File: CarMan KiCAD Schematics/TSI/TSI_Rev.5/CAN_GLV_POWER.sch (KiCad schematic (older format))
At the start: 52 parts, among them J31 Cooling Jumper, K2 G5LE-1-E, K3 SFS2-DC24V, K4 SFS2-DC24V, Q11 TN2130K1-G, U14 Bottom Left, U15 Top Left, U17 Top Right, U2 Bottom Right, U20 TLP293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

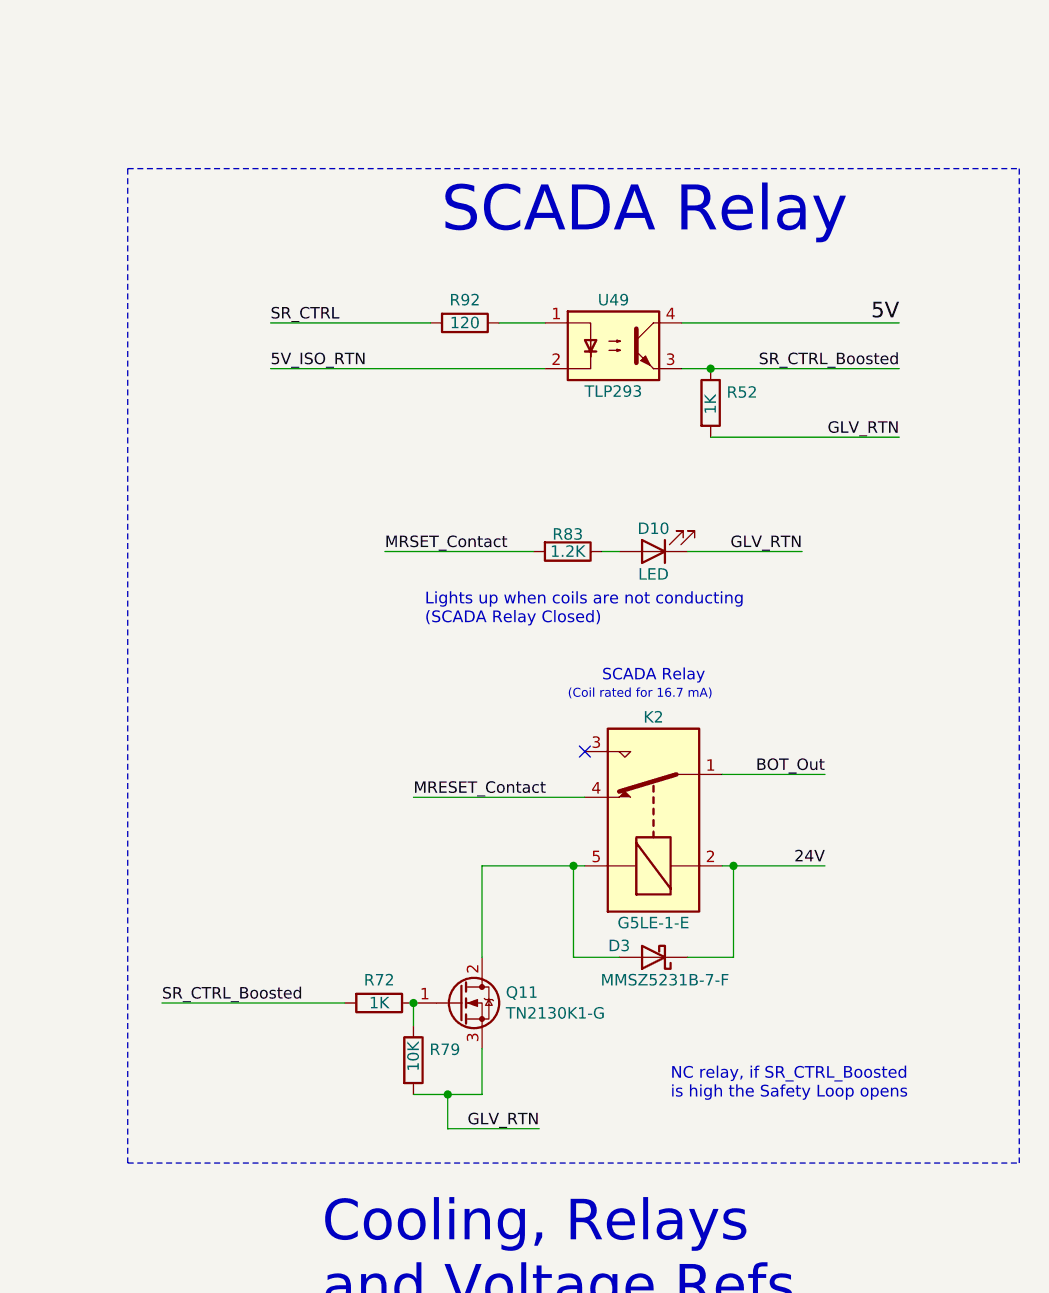
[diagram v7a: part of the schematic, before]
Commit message: - SR Control boosted and scada relay circuit edited
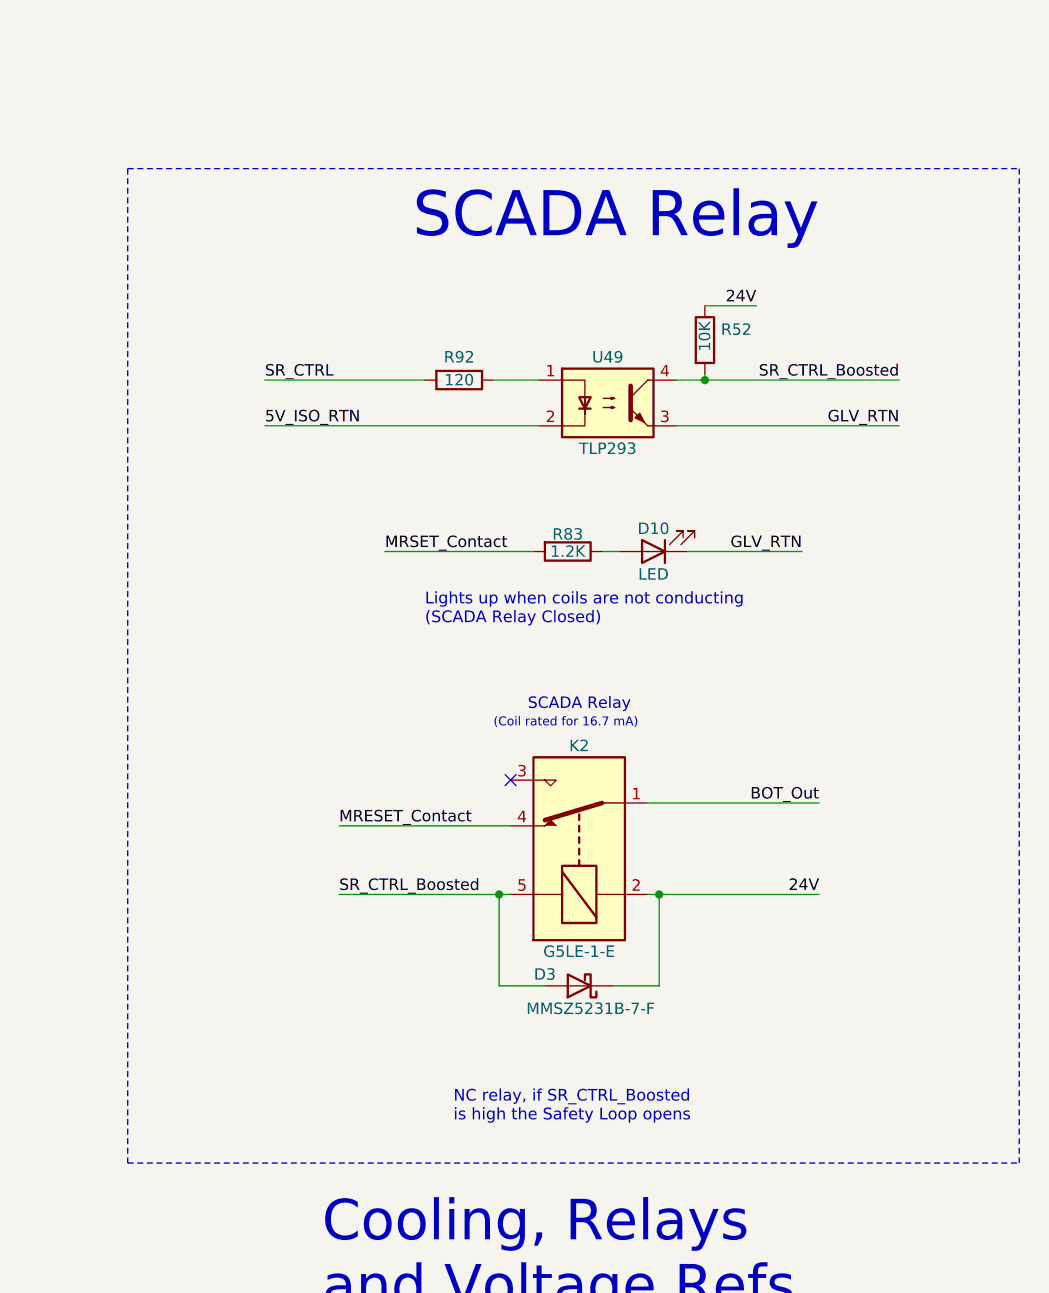
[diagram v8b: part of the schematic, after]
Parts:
- removed Q11: TN2130K1-G, TSI_Rev_2021_Footprint_Lib:SOT95P237X112-3N, symbol Device:Q_NMOS_GDS
- removed R72: 1K, Resistor_SMD:R_0805_2012Metric_Pad1.15x1.40mm_HandSolder, symbol Device:R
- removed R79: 10K, Resistor_SMD:R_0805_2012Metric_Pad1.15x1.40mm_HandSolder, symbol Device:R
- R52: value 1K -> 10K
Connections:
- wire segments 204 -> 197
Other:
- moved on the sheet: D3, K2, R52, R92, U49
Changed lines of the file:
@@
 Text Notes 12900 10500 0    177  ~ 0
 Cooling, Relays \nand Voltage Refs\n
-Text Label 12675 6175 0    50   ~ 0
+Text Label 12650 6425 0    50   ~ 0
 SR_CTRL
 $Comp
 L Device:D_Schottky D3
 U 1 1 5FB8F043
-P 14350 8950
-F 0 "D3" H 14500 8900 50  0000 C CNN
-F 1 "MMSZ5231B-7-F" H 14300 9050 50  0000 C CNN
-F 2 "Diode_SMD:D_SOD-123" H 14350 8950 50  0001 C CNN
-F 3 "~" H 14350 8950 50  0001 C CNN
-	1    14350 8950
+P 14025 9075
+F 0 "D3" H 14175 9025 50  0000 C CNN
+F 1 "MMSZ5231B-7-F" H 13975 9175 50  0000 C CNN
+F 2 "Diode_SMD:D_SOD-123" H 14025 9075 50  0001 C CNN
+F 3 "~" H 14025 9075 50  0001 C CNN
+	1    14025 9075
 	-1   0    0    1
 $EndComp
 Wire Wire Line
-	14650 8550 14700 8550
-NoConn ~ 14050 8050
+	14325 8675 14375 8675
+NoConn ~ 13725 8175
 Text Notes 14800 750  0    98   ~ 0
 SIGNALS
@@
 Wire Notes Line
 	2250 3950 4000 3950
-Text Label 12675 6375 0    50   ~ 0
+Text Label 12650 6625 0    50   ~ 0
 5V_ISO_RTN
 $Comp
 L TSI_Rev.5-rescue:TLP293-CarMan_KiCAD_Library-TSI_Rev.5-rescue U49
 U 1 1 5FA61B5B
-P 14175 6275
-F 0 "U49" H 14175 6475 50  0000 C CNN
-F 1 "TLP293" H 14175 6075 50  0000 C CNN
-F 2 "Package_SO:SOIC-4_4.55x2.6mm_P1.27mm" H 13975 6075 50  0001 L CIN
-F 3 "" H 14175 6275 50  0001 L CNN
-	1    14175 6275
-	1    0    0    -1
-$EndComp
-Wire Wire Line
-	13875 6175 13675 6175
+P 14150 6525
+F 0 "U49" H 14150 6725 50  0000 C CNN
+F 1 "TLP293" H 14150 6325 50  0000 C CNN
+F 2 "Package_SO:SOIC-4_4.55x2.6mm_P1.27mm" H 13950 6325 50  0001 L CIN
+F 3 "" H 14150 6525 50  0001 L CNN
+	1    14150 6525
+	1    0    0    -1
+$EndComp
+Wire Wire Line
+	13850 6425 13650 6425
 $Comp
 L Device:R R92
 U 1 1 5FA61B65
-P 13525 6175
-F 0 "R92" V 13425 6175 50  0000 C CNN
-F 1 "120" V 13525 6175 50  0000 C CNN
-F 2 "Resistor_SMD:R_0805_2012Metric_Pad1.15x1.40mm_HandSolder" V 13455 6175 50  0001 C CNN
-F 3 "~" H 13525 6175 50  0001 C CNN
-	1    13525 6175
+P 13500 6425
+F 0 "R92" V 13400 6425 50  0000 C CNN
+F 1 "120" V 13500 6425 50  0000 C CNN
+F 2 "Resistor_SMD:R_0805_2012Metric_Pad1.15x1.40mm_HandSolder" V 13430 6425 50  0001 C CNN
+F 3 "~" H 13500 6425 50  0001 C CNN
+	1    13500 6425
 	0    1    1    0
 $EndComp
-Text Notes 14125 7750 0    50   ~ 0
+Text Notes 13800 7875 0    50   ~ 0
 SCADA Relay\n
-$Comp
-L Device:Q_NMOS_GDS Q11
-U 1 1 5FB4C495
-P 13500 9150
-F 0 "Q11" H 13704 9196 50  0000 L CNN
-F 1 "TN2130K1-G" H 13704 9105 50  0000 L CNN
-F 2 "TSI_Rev_2021_Footprint_Lib:SOT95P237X112-3N" H 13700 9250 50  0001 C CNN
-F 3 "https://ww1.microchip.com/downloads/en/DeviceDoc/TN2130-N-Channel-Enhancement-Mode-Vertical-DMOS-FET-Data-Sheet-20005944B.pdf" H 13500 9150 50  0001 C CNN
-	1    13500 9150
-	1    0    0    -1
-$EndComp
-Text Label 12200 9150 0    50   ~ 0
+Text Label 12975 8675 0    50   ~ 0
 SR_CTRL_Boosted
 $Comp
@@
 Text Label 3350 1250 0    50   ~ 0
 5V_ISO_RTN
-Text Label 13300 8250 0    50   ~ 0
+Text Label 12975 8375 0    50   ~ 0
 MRESET_Contact
 Text Notes 6275 800  2    89   ~ 0
 Cooling Control & Sensors\n
-$Comp
-L Device:R R72
-U 1 1 5FB6696B
-P 13150 9150
-F 0 "R72" V 13050 9150 50  0000 C CNN
-F 1 "1K" V 13150 9150 50  0000 C CNN
-F 2 "Resistor_SMD:R_0805_2012Metric_Pad1.15x1.40mm_HandSolder" V 13080 9150 50  0001 C CNN
-F 3 "~" H 13150 9150 50  0001 C CNN
-	1    13150 9150
-	0    1    1    0
-$EndComp
-Wire Wire Line
-	13300 9150 13300 9250
-Text Label 13850 9700 2    50   ~ 0
-GLV_RTN
-Connection ~ 13300 9150
-Wire Wire Line
-	13600 9350 13600 9550
-Wire Wire Line
-	13600 9550 13450 9550
-Wire Wire Line
-	13600 8950 13600 8550
-Text Label 15100 8550 2    50   ~ 0
+Text Label 15075 8675 2    50   ~ 0
 24V
 Wire Wire Line
-	14500 8950 14700 8950
-Connection ~ 14700 8550
-Wire Wire Line
-	14200 8950 14000 8950
-Connection ~ 14000 8550
-Wire Wire Line
-	14000 8550 14050 8550
+	14175 9075 14375 9075
+Wire Wire Line
+	13875 9075 13675 9075
+Wire Wire Line
+	13675 8675 13725 8675
 Text Notes 11050 11200 0    39   ~ 0
 Zacky Bear Doesn't Like
@@
 L Device:R R52
 U 1 1 5FC2D02C
-P 14600 6525
-F 0 "R52" H 14670 6571 50  0000 L CNN
-F 1 "1K" V 14600 6475 50  0000 L CNN
-F 2 "Resistor_SMD:R_0805_2012Metric_Pad1.15x1.40mm_HandSolder" V 14530 6525 50  0001 C CNN
-F 3 "~" H 14600 6525 50  0001 C CNN
-	1    14600 6525
-	1    0    0    -1
-$EndComp
-Text Label 15425 6175 2    68   ~ 0
-5V
-Wire Wire Line
-	12675 6375 13875 6375
-Wire Wire Line
-	12675 6175 13375 6175
+P 14575 6250
+F 0 "R52" H 14645 6296 50  0000 L CNN
+F 1 "10K" V 14575 6200 50  0000 L CNN
+F 2 "Resistor_SMD:R_0805_2012Metric_Pad1.15x1.40mm_HandSolder" V 14505 6250 50  0001 C CNN
+F 3 "~" H 14575 6250 50  0001 C CNN
+	1    14575 6250
+	1    0    0    -1
+$EndComp
+Wire Wire Line
+	12650 6625 13850 6625
+Wire Wire Line
+	12650 6425 13350 6425
 Wire Wire Line
 	3350 1050 3850 1050
@@
 Wire Wire Line
 	4950 1050 5900 1050
-Wire Wire Line
-	13450 9550 13450 9700
-Wire Wire Line
-	13450 9700 13850 9700
-Connection ~ 13450 9550
-Wire Wire Line
-	13450 9550 13300 9550
-Wire Wire Line
-	12200 9150 13000 9150
 Text Label 4625 9300 2    50   ~ 0
 IMD_Status
@@
 L TSI_Rev.5-rescue:G5LE-1-E-Lafayette_Electric_Car_Internals RL?
 U 1 1 5FB466B1
-P 14350 8350
+P 14025 8475
 AR Path="/5FB466B1" Ref="RL?"  Part="1"
 AR Path="/5FE1DE7D/5FB466B1" Ref="K2"  Part="1"
-F 0 "K2" V 14800 8350 50  0000 C CNN
-F 1 "G5LE-1-E" V 13900 8350 50  0000 C CNN
-F 2 "TSI_Rev_2021_Footprint_Lib:G5LE-1-E DC24" H 14600 8950 50  0001 C CNN
-F 3 "https://media.digikey.com/pdf/Data%20Sheets/Omron%20PDFs/G5LE-E_G.pdf" H 14600 8950 50  0001 C CNN
-	1    14350 8350
+F 0 "K2" V 14475 8475 50  0000 C CNN
+F 1 "G5LE-1-E" V 13575 8475 50  0000 C CNN
+F 2 "TSI_Rev_2021_Footprint_Lib:G5LE-1-E DC24" H 14275 9075 50  0001 C CNN
+F 3 "https://media.digikey.com/pdf/Data%20Sheets/Omron%20PDFs/G5LE-E_G.pdf" H 14275 9075 50  0001 C CNN
+	1    14025 8475
 	0    -1   -1   0
 $EndComp
-Wire Wire Line
-	15100 8150 14650 8150
-Text Label 15100 8150 2    50   ~ 0
+Text Label 15075 8275 2    50   ~ 0
 BOT_Out
 Wire Wire Line
-	13300 8250 14050 8250
+	12975 8375 13725 8375
 Wire Wire Line
 	7300 8925 6700 8925
@@
 Wire Notes Line
 	12050 9850 15950 9850
-Text Notes 15200 5800 2    197  ~ 0
+Text Notes 15075 5825 2    197  ~ 0
 SCADA Relay
 Wire Notes Line
@@
 Wire Notes Line
 	15950 5500 15950 9850
-Wire Wire Line
-	14475 6375 14600 6375
-Text Label 15425 6375 2    50   ~ 0
-SR_CTRL_Boosted
-Connection ~ 14600 6375
-Wire Wire Line
-	14600 6375 15425 6375
-Text Label 15425 6675 2    50   ~ 0
-GLV_RTN
-Wire Wire Line
-	14600 6675 15425 6675
-Wire Wire Line
-	14475 6175 15425 6175
 $Comp
 L Device:LED D9
@@
 Wire Wire Line
 	14125 7175 14200 7175
-Text Notes 14425 9575 0    51   ~ 0
+Text Notes 13475 9675 0    51   ~ 0
 NC relay, if SR_CTRL_Boosted \nis high the Safety Loop opens
 Text Label 7900 1375 0    50   ~ 0
@@
 Wire Wire Line
 	10625 3325 11325 3325
-$Comp
-L Device:R R79
-U 1 1 5FB66337
-P 13300 9400
-F 0 "R79" H 13370 9446 50  0000 L CNN
-F 1 "10K" V 13300 9350 50  0000 L CNN
-F 2 "Resistor_SMD:R_0805_2012Metric_Pad1.15x1.40mm_HandSolder" V 13230 9400 50  0001 C CNN
-F 3 "~" H 13300 9400 50  0001 C CNN
-	1    13300 9400
-	1    0    0    -1
-$EndComp
-Text Notes 13975 7825 0    39   ~ 0
+Text Notes 13650 7950 0    39   ~ 0
 (Coil rated for 16.7 mA)
 Wire Wire Line
-	14700 8550 14700 8950
-Wire Wire Line
-	14000 8550 14000 8950
-Wire Wire Line
-	14700 8550 15100 8550
+	14375 8675 14375 9075
+Wire Wire Line
+	13675 8675 13675 9075
 Text Notes 12400 3150 0    39   ~ 0
 Needs to be\nrated for 1/2W\n
-Wire Wire Line
-	13600 8550 14000 8550
 Text Label 10750 2300 0    50   ~ 0
 AIRs-
@@
 Wire Notes Line
 	5800 3800 5800 6350
+Text Label 15425 6625 2    50   ~ 0
+GLV_RTN
+Wire Wire Line
+	14450 6425 14575 6425
+Wire Wire Line
+	14575 6425 14575 6400
+Text Label 14800 6100 2    50   ~ 0
+24V
+Wire Wire Line
+	14575 6100 14800 6100
+Text Label 15425 6425 2    50   ~ 0
+SR_CTRL_Boosted
+Connection ~ 14575 6425
+Wire Wire Line
+	14450 6625 15425 6625
+Wire Wire Line
+	14575 6425 15425 6425
+Wire Wire Line
+	13675 8675 12975 8675
+Connection ~ 13675 8675
+Wire Wire Line
+	14325 8275 15075 8275
+Wire Wire Line
+	14375 8675 15075 8675
+Connection ~ 14375 8675
 $EndSCHEMATC
